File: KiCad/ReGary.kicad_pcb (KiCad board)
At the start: 4 copper layers, 38 x 38 mm, 36 parts, among them U1 GW1N-UV1P5LQ100, U2 LM1117-3.3, U3 SN74CBTD16210, U4 SN74CBTD16210, U5 SN74CBTD16210, U6 SN74CBTD16210, U7 PLCC_84_plug, U8 PLCC_84_plug

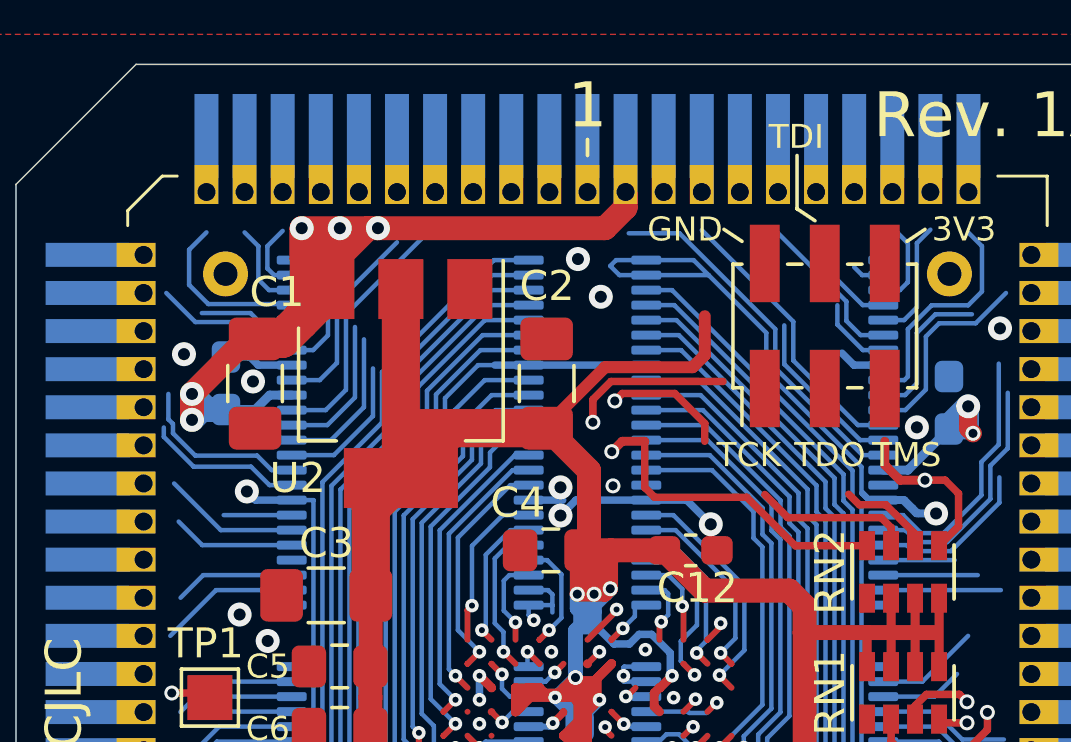
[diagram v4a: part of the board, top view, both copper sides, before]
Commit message: Fix placement of VCC vias, C1 and U2 voltage regulator
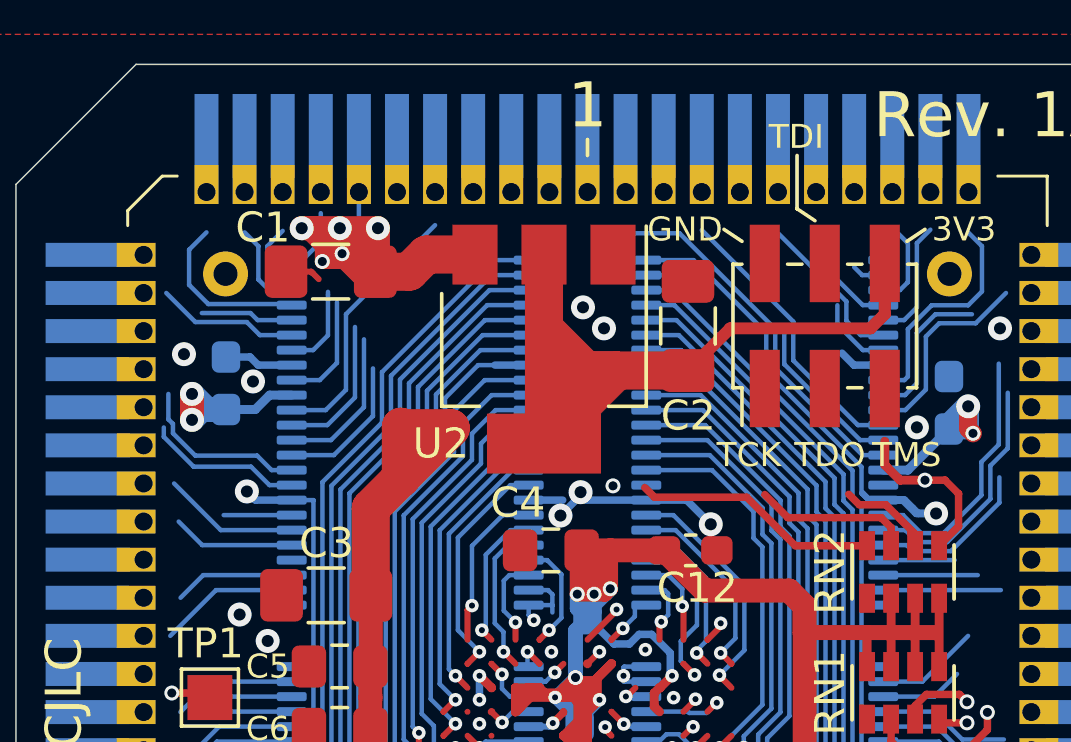
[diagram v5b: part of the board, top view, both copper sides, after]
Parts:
- moved C2 5.09 mm to (147.8, 64.1)
- moved U2 4.91 mm to (143.0, 64.9)
- moved C1 4.50 mm to (135.9, 62.3), turned to 0 degrees
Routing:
- net VCC: track 58.5 -> 44.5 mm, vias 11 -> 13
- net TMS: track 18.9 -> 8.94 mm, vias 2 -> 1
- net 3V3: track 199.7 -> 206.7 mm
- net TDO: track 20.9 -> 16.8 mm, vias 2 -> 1
- net RW: track 6.60 -> 3.77 mm
- net TCK: track 19.5 -> 16.7 mm, vias 2 -> 1
- net Net-(U8-Pad7): track 0.00 -> 2.40 mm
- net SIZ0: track 4.93 -> 2.86 mm
- net GND: track 125.7 -> 126.9 mm
- net SIZ1: track 1.06 -> 2.17 mm

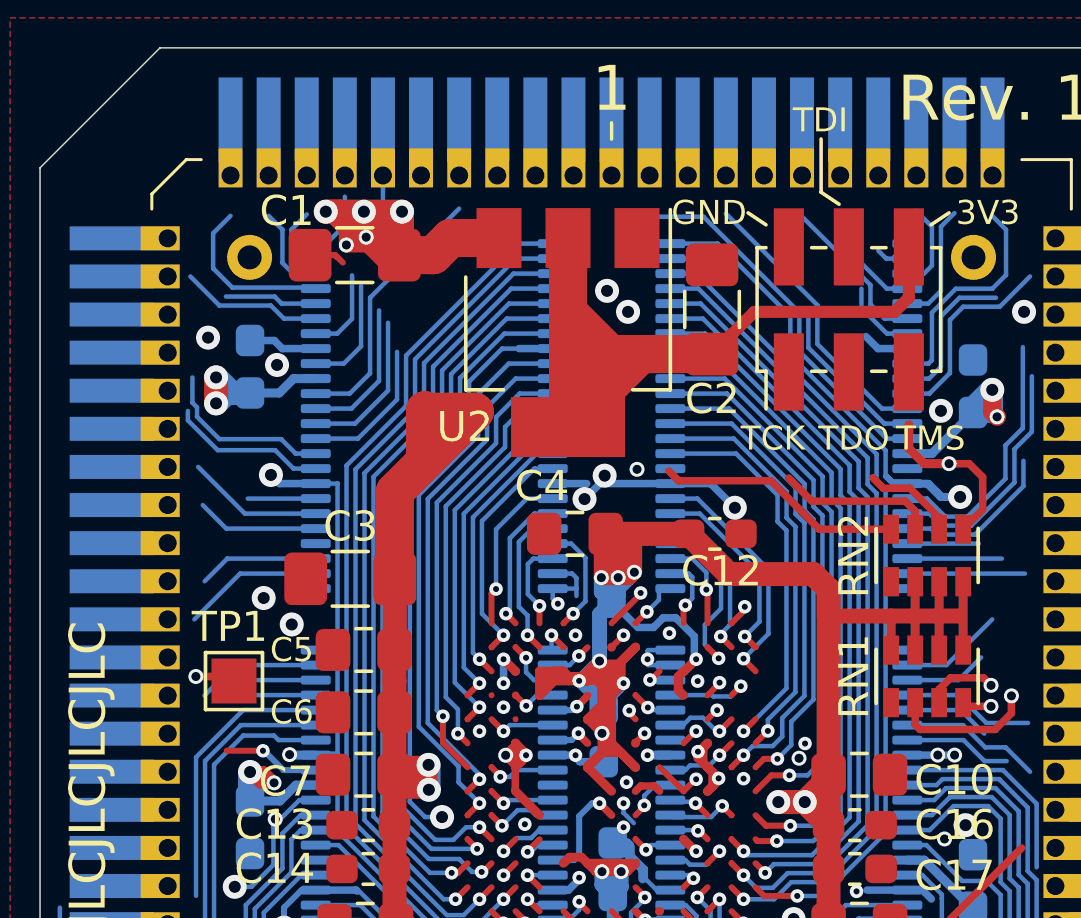
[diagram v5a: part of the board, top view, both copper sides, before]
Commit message: Add a 4V3 LDO voltage regulator
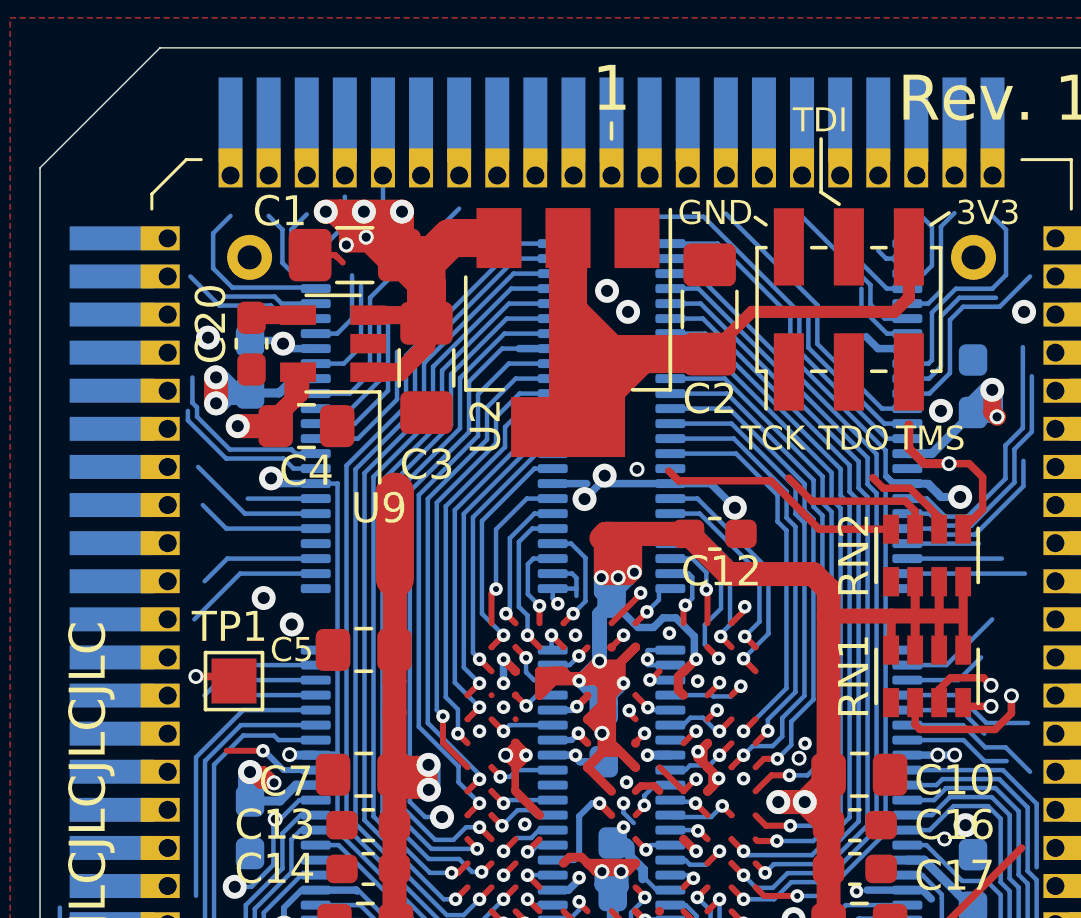
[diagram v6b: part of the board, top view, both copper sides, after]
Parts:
- added U9: TPS73643DBV, Package_TO_SOT_SMD:SOT-23-5, F.Cu at (135.2, 65.3)
- C20: renamed from C6; footprint Capacitor_SMD:C_0805_2012Metric_Pad1.15x1.40mm_HandSolder -> Capacitor_SMD:C_0603_1608Metric_Pad1.08x0.95mm_HandSolder
- moved C20 12.8 mm to (132.4, 65.3), turned to 270 degrees
- moved C4 9.64 mm to (134.3, 68.0), turned to 180 degrees
- moved C3 7.47 mm to (138.3, 66.1), turned to 90 degrees
- moved C2 0.08 mm to (147.7, 64.1)
- renumbered C20 to C6
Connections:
- C20 pad 1: GND -> Net-(C20-Pad1)
- C20 pad 2: 3V3 -> GND
- C3 pad 2: 3V3 -> VCC
- C4 pad 2: 3V3 -> 4V3
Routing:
- net VCC: track 44.5 -> 55.5 mm
- net 3V3: track 206.7 -> 199.5 mm
- net 4V3: track 0.00 -> 5.10 mm, vias 0 -> 1
- net Net-(C20-Pad1): track 0.00 -> 1.66 mm

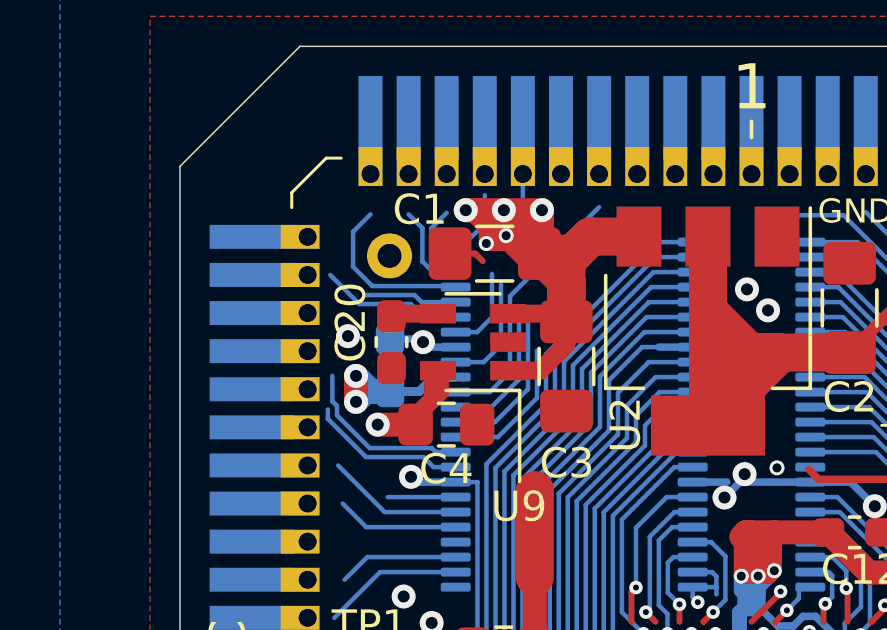
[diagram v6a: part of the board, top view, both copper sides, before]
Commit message: Change level shifters from CBTD to CBT with 4V3 power supply, change inner power layer from VCC to 4V3
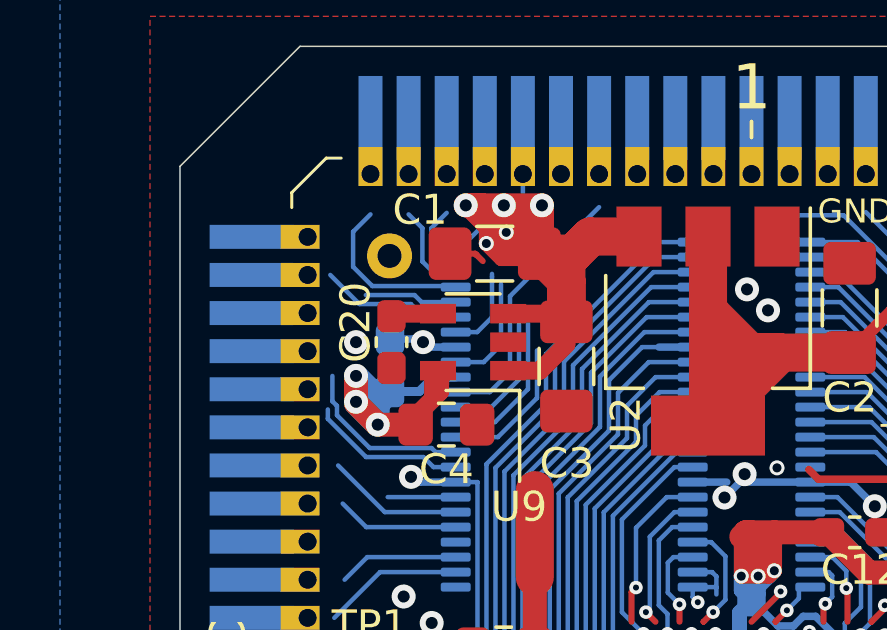
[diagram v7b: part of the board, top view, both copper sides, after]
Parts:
- U3, U4, U5, U6: value SN74CBTD16210 -> SN74CBT16210
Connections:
- C21 pad 2: VCC -> 4V3
- C22 pad 2: VCC -> 4V3
- C23 pad 2: VCC -> 4V3
- C24 pad 2: VCC -> 4V3
- U3 pad 15: VCC -> 4V3
- U4 pad 15: VCC -> 4V3
- U5 pad 15: VCC -> 4V3
- U6 pad 15: VCC -> 4V3
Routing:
- net VCC: track 55.5 -> 95.4 mm, vias 13 -> 5
- net 4V3: track 5.10 -> 37.1 mm, vias 1 -> 9
- added copper zone on 4V3.Cu, net 3V3
- added copper zone on 4V3.Cu, net 4V3
- removed copper zone on VCC.Cu, net 3V3
- removed copper zone on VCC.Cu, net VCC

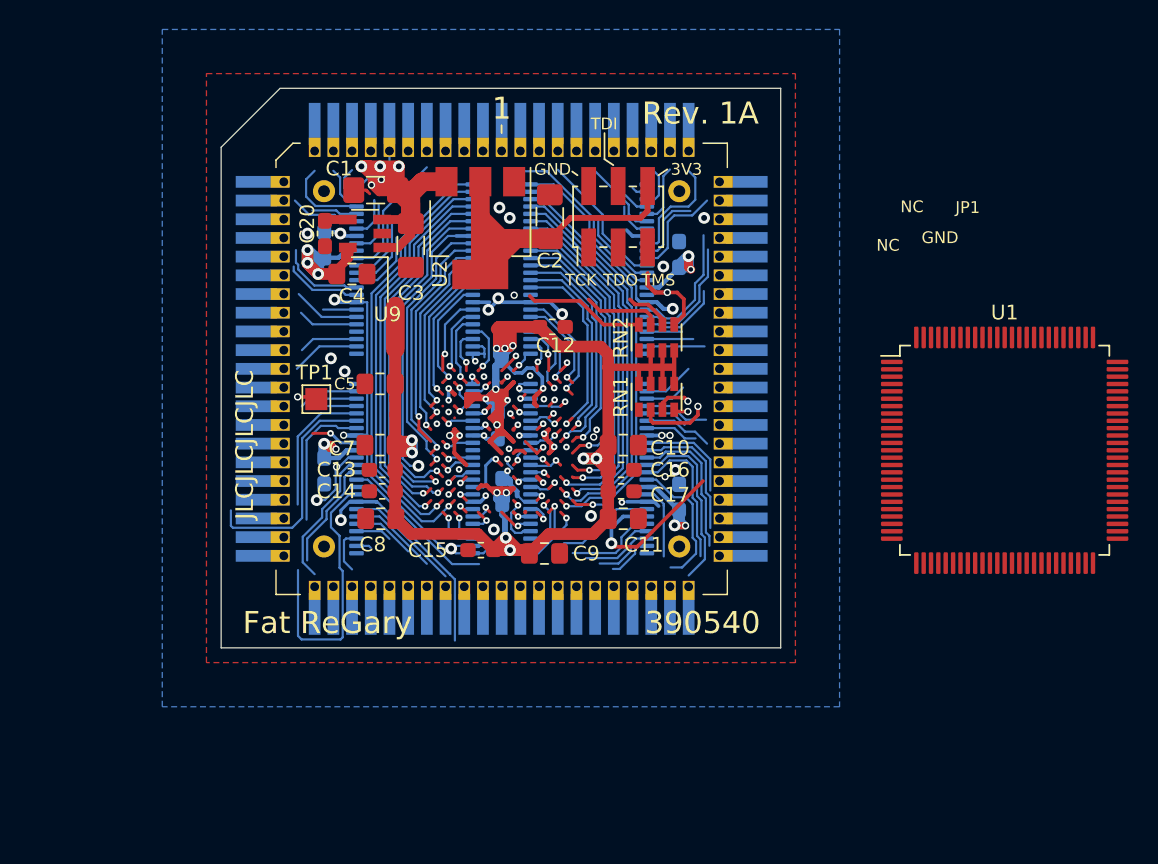
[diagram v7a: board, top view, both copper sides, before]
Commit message: Fixed placement of C5 and FPGA, more cleanup of old vias and traces
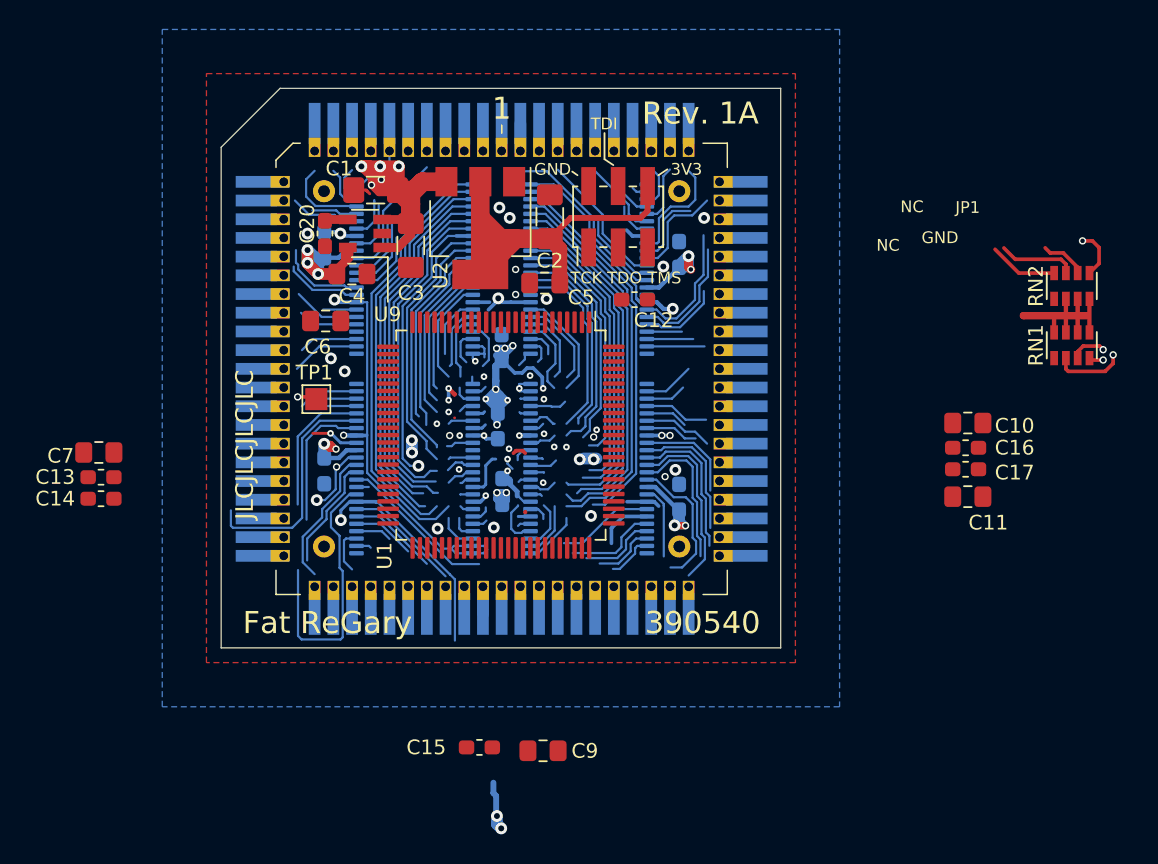
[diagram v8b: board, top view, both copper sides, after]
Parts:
- moved U1 34.2 mm to (144.4, 79.0), turned to 270 degrees
- moved RN1 28.4 mm to (183.2, 72.9)
- moved RN2 28.4 mm to (183.2, 68.8)
- moved C10 23.4 mm to (176.1, 78.1)
- moved C11 23.4 mm to (176.1, 83.1)
- moved C16 23.4 mm to (176.0, 79.8)
- moved C17 23.4 mm to (176.0, 81.3)
- moved C13 19.1 mm to (117.2, 81.8)
- moved C14 19.1 mm to (117.2, 83.3)
- moved C7 19.1 mm to (117.1, 80.1)
- moved C6 13.9 mm to (132.5, 71.2)
- moved C9 13.4 mm to (147.3, 100.4)
- moved C15 13.4 mm to (142.9, 100.2)
- moved C5 13.1 mm to (147.4, 68.6)
- moved C12 5.88 mm to (153.5, 69.8)
- renumbered C8 to C6, C6 to C8
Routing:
- net 3V3: track 199.5 -> 76.9 mm
- net CLK90: track 11.9 -> 3.76 mm, vias 1 -> 0
- net TCK: track 16.7 -> 11.4 mm, vias 1 -> 0
- net VCC: track 95.4 -> 99.1 mm
- net TDO: track 16.8 -> 13.5 mm, vias 1 -> 0
- net TDI: track 20.7 -> 18.0 mm, vias 2 -> 1
- net GND: track 126.9 -> 124.4 mm, vias 46 -> 45
- net A1_FPGA: track 15.1 -> 13.1 mm, vias 1 -> 0
- net nCONFIG: track 14.7 -> 12.8 mm, vias 2 -> 1
- net EBR2_FPGA: track 27.4 -> 25.9 mm, vias 1 -> 0
- net MS2_FPGA: track 2.49 -> 0.99 mm, vias 1 -> 0
- net TMS: track 8.94 -> 7.53 mm, vias 1 -> 0
- net EBG0_FPGA: track 18.1 -> 16.7 mm, vias 1 -> 0
- net ABOE1_FPGA: track 20.6 -> 19.3 mm, vias 1 -> 0
- net CIIN_FPGA: track 5.51 -> 4.30 mm, vias 1 -> 0
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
